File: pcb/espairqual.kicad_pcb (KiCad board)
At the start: 2 copper layers, 81 x 50 mm, 33 parts, among them J1 24VAC, J2 PMSX003, J7 eflashy32, U1 BD9G101G, U2 ESP32-S2-WROVER, U3 AP1117-33

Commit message: hmm
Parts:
- added J3: USB_C_Receptacle_USB2.0, Connector_USB:USB_C_Receptacle_HRO_TYPE-C-31-M-12, F.Cu at (85.6, 76.2)
- added R4: 5k1, Resistor_SMD:R_0805_2012Metric, F.Cu at (77.8, 74.0)
- added R7: 5k1, Resistor_SMD:R_0805_2012Metric, F.Cu at (93.2, 74.0)
- moved L1 0.98 mm to (51.2, 67.6)
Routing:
- net +5V: track 136.8 -> 147.6 mm, vias 3 -> 5
- net GND: track 106.4 -> 117.2 mm, vias 26 -> 30
- net Net-(J3-PadA5): track 0.00 -> 10.7 mm
- net Net-(J3-PadB5): track 0.00 -> 9.93 mm

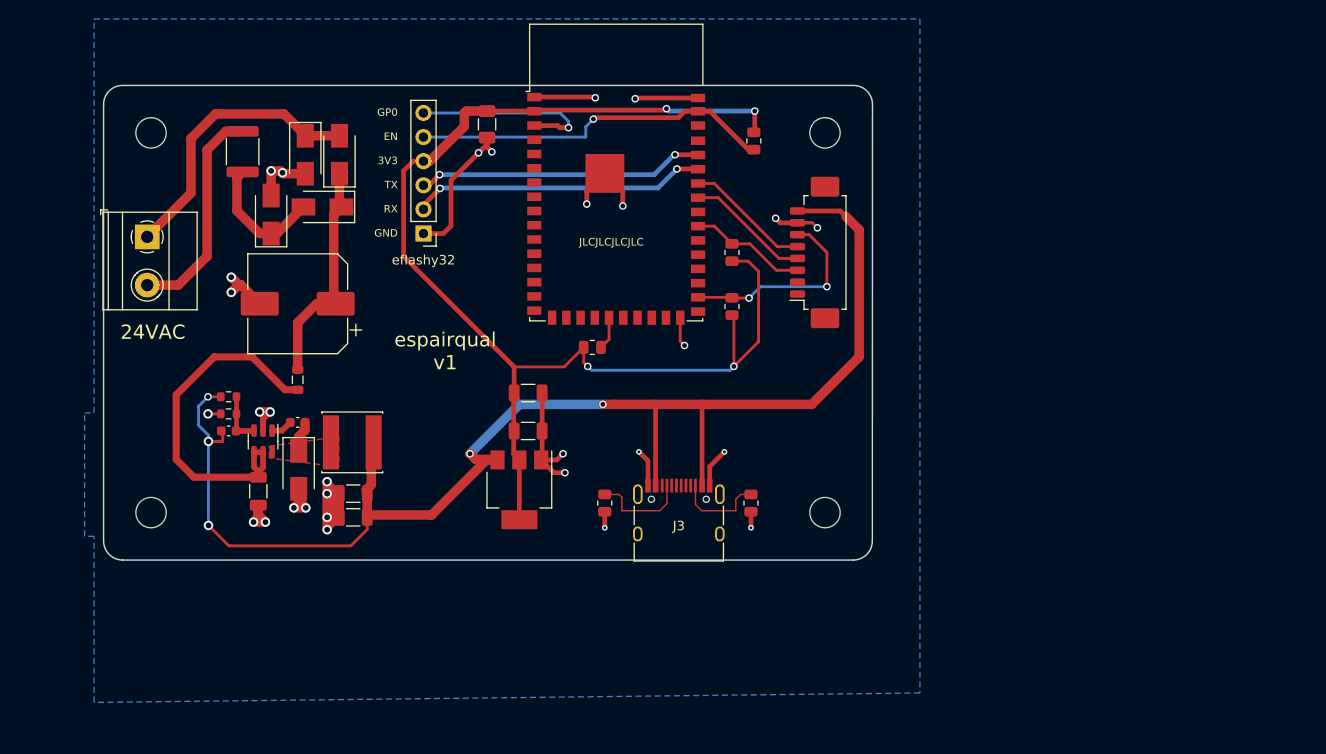
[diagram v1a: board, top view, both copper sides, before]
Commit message: esp32 time
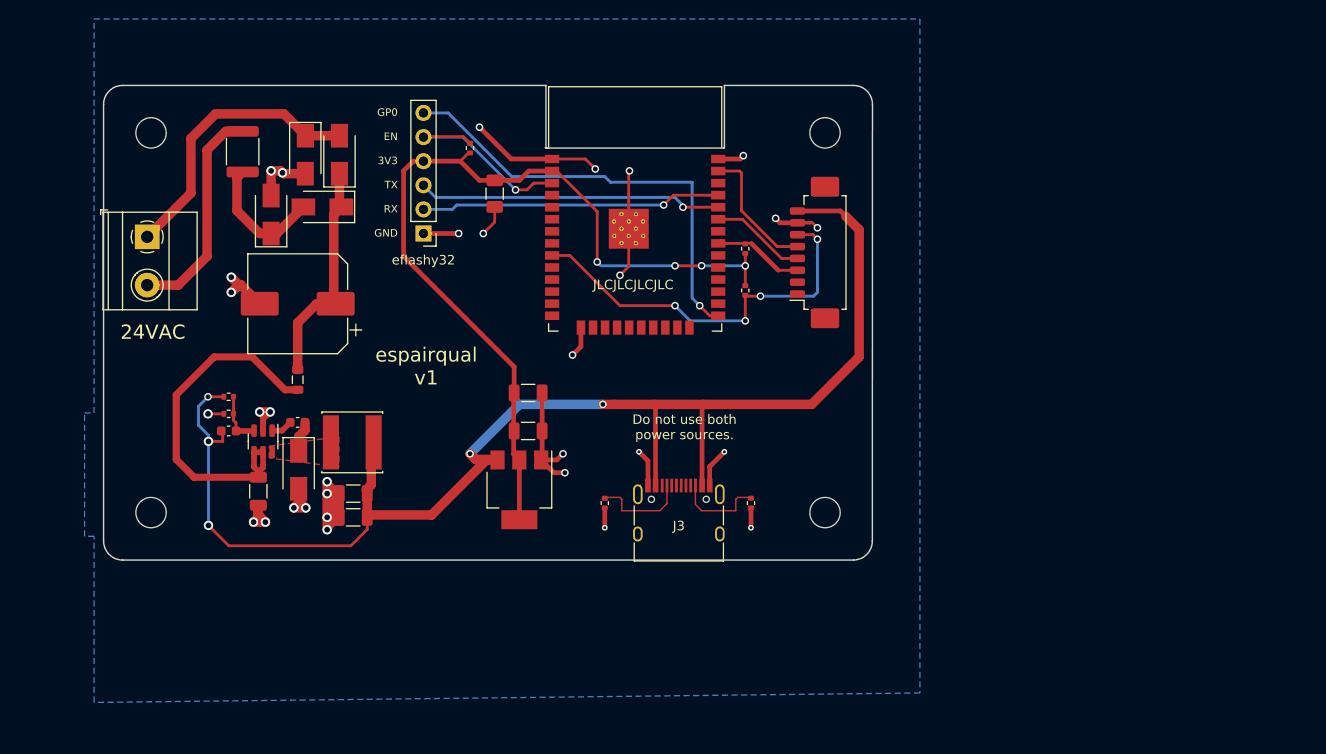
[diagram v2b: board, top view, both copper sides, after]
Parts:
- removed R6: 10K, Resistor_SMD:R_0805_2012Metric
- R1, R3, R4, R5, R7: footprint Resistor_SMD:R_0805_2012Metric -> Resistor_SMD:R_0402_1005Metric
- R12, R2: footprint Resistor_SMD:R_0603_1608Metric -> Resistor_SMD:R_0402_1005Metric
- U2: value ESP32-S2-WROVER -> ESP32-WROOM-32D; footprint RF_Module:ESP32-S2-WROVER -> RF_Module:ESP32-WROOM-32
- U3: value AP1117-33 -> AMS1117-3.3
- moved R5 29.9 mm to (63.6, 36.6), turned to -90 degrees
- moved C7 7.34 mm to (66.2, 41.4)
- moved U2 3.61 mm to (81.0, 46.0)
- moved R3 2.19 mm to (92.6, 51.6), turned to 90 degrees
- moved R1 1.46 mm to (92.6, 47.2)
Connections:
- U2 pad 15: unconnected-(U2-Pad15) -> GND
- U2 pad 21: Net-(R6-Pad1) -> unconnected-(U2-Pad21)
- U2 pad 25: unconnected-(U2-Pad25) -> /GPIO0
- U2 pad 26: GND -> unconnected-(U2-Pad26)
- U2 pad 28: /PMS_SET -> unconnected-(U2-Pad28)
- U2 pad 3: /GPIO0 -> /EN
- U2 pad 31: unconnected-(U2-Pad31) -> /PMS_RESET
- U2 pad 33: /PMS_RESET -> /PMS_TXD
- U2 pad 34: unconnected-(U2-Pad34) -> /TX
- U2 pad 35: /PMS_TXD -> /RX
- U2 pad 36: /PMS_RXD -> unconnected-(U2-Pad36)
- U2 pad 37: /RX -> /PMS_RXD
- U2 pad 38: /TX -> GND
- U2 pad 39: unconnected-(U2-Pad39) -> GND
- U2 pad 9: unconnected-(U2-Pad9) -> /PMS_SET
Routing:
- net +3V3: track 130.7 -> 91.5 mm
- net /GPIO0: track 20.0 -> 47.0 mm
- net /PMS_SET: track 21.6 -> 41.6 mm, vias 2 -> 4
- net /EN: track 38.2 -> 21.3 mm
- net Net-(R6-Pad1): track 3.48 -> 0.00 mm
- net /PMS_TXD: track 13.1 -> 10.1 mm
- net /PMS_RESET: track 12.4 -> 9.52 mm
- net /TX: track 30.3 -> 32.1 mm, vias 2 -> 1
- net GND: track 117.2 -> 116.2 mm, vias 30 -> 31
- net /PMS_RXD: track 13.2 -> 14.0 mm
- net /RX: track 31.0 -> 31.7 mm, vias 2 -> 1
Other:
- outline, holes or cut-outs redrawn
- board text added: "Do not use both power sources."

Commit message: caps
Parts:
- added C10: 10uF 50V, Capacitor_SMD:C_1206_3216Metric, F.Cu at (43.0, 50.1)
- added C11: 10uF 50V, Capacitor_SMD:C_1206_3216Metric, F.Cu at (40.4, 50.1)
- added C12: 10uF 50V, Capacitor_SMD:C_1206_3216Metric, F.Cu at (48.2, 50.1)
- C6: value 470uF 50V -> 10uF 50V; footprint Capacitor_SMD:CP_Elec_10x10 -> Capacitor_SMD:C_1206_3216Metric
- moved FB1 11.1 mm to (37.6, 53.2)
- moved R7 6.21 mm to (89.8, 68.8)
- moved C8 6.21 mm to (66.3, 61.2)
- moved J3 6.21 mm to (82.2, 71.0)
- moved R4 6.21 mm to (74.4, 68.8)
- moved C9 6.21 mm to (66.3, 57.2)
- moved U3 6.21 mm to (65.4, 67.4)
- moved REF** 5.20 mm to (101.0, 69.8)
- moved REF** 5.20 mm to (30.0, 69.8)
- moved C4 5.18 mm to (38.2, 61.2)
- moved C1 5.17 mm to (41.3, 67.6)
- moved C2 5.17 mm to (51.3, 70.3)
- moved C3 5.17 mm to (51.3, 67.8)
- moved C5 5.17 mm to (45.5, 60.3)
- moved D1 5.17 mm to (45.5, 65.3)
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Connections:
- net Net-(C6-Pad1) renamed /Vrec
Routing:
- net Net-(C1-Pad1): track 37.6 -> 28.1 mm
- net +3V3: track 91.5 -> 84.9 mm
- net +5V: track 147.6 -> 141.4 mm
- net GND: track 116.2 -> 121.0 mm
- net /Vrec: track 24.0 -> 25.0 mm
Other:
- board size 81 x 50 mm -> 81 x 44.8 mm

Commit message: update workflow
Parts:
- removed C11, C12: 10uF 50V, Capacitor_SMD:C_1206_3216Metric
- removed REF** (x4): MountingHole_3.2mm_M3, MountingHole:MountingHole_3.2mm_M3
- added C16: 1uF, Capacitor_SMD:C_0603_1608Metric, F.Cu at (71.5, 44.8)
- added H1: MountingHole, MountingHole:MountingHole_3.2mm_M3, F.Cu at (30.0, 75.2)
- added H2: MountingHole, MountingHole:MountingHole_3.2mm_M3, F.Cu at (101.2, 75.2)
- added H3: MountingHole, MountingHole:MountingHole_3.2mm_M3, F.Cu at (30.0, 34.6)
- added H4: MountingHole, MountingHole:MountingHole_3.2mm_M3, F.Cu at (101.2, 34.6)
- C10: value 10uF 50V -> 100uF 50V; footprint Capacitor_SMD:C_1206_3216Metric -> Capacitor_THT:CP_Radial_D10.0mm_P5.00mm_P7.50mm
- moved J2 29.1 mm to (89.0, 74.3), turned to 0 degrees
- moved R7 20.3 mm to (69.5, 68.9), turned to 90 degrees
- moved J1 20.1 mm to (46.1, 34.5), turned to 180 degrees
- moved J3 15.4 mm to (67.9, 76.7)
- moved C10 9.48 mm to (50.0, 56.5)
- moved C6 8.62 mm to (40.3, 56.9)
- moved R4 7.80 mm to (66.6, 68.9), turned to 90 degrees
- moved C8 7.74 mm to (69.8, 54.3)
- moved C9 7.74 mm to (69.8, 50.3)
- moved U3 7.74 mm to (68.9, 60.5)
- moved D3 6.79 mm to (47.5, 49.6)
- moved D4 6.79 mm to (45.8, 44.1)
- moved D5 6.79 mm to (49.4, 44.1)
- moved L1 6.79 mm to (50.7, 69.2)
- moved R12 6.79 mm to (37.7, 64.4)
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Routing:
- net /PMS_RXD: track 14.0 -> 47.8 mm, vias 0 -> 2
- net GND: track 121.0 -> 87.3 mm, vias 31 -> 30
- net /PMS_TXD: track 10.1 -> 42.2 mm, vias 0 -> 2
- net /PMS_RESET: track 9.52 -> 39.4 mm, vias 0 -> 2
- net Net-(D4-Pad1): track 30.0 -> 11.3 mm
- net Net-(F1-Pad1): track 23.3 -> 7.91 mm
- net +3V3: track 84.9 -> 74.6 mm
- net +5V: track 141.4 -> 131.7 mm, vias 5 -> 7
- net Net-(J3-PadA5): track 10.5 -> 2.57 mm
- net Net-(J3-PadB5): track 9.83 -> 2.61 mm
- net /Vrec: track 25.0 -> 29.1 mm
- net /PMS_SET: track 41.6 -> 45.6 mm, vias 4 -> 2
- net /GPIO0: track 47.0 -> 43.4 mm
- net /RX: track 31.7 -> 28.9 mm
- net /TX: track 32.1 -> 29.5 mm
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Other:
- board size 81 x 44.8 mm -> 98 x 50 mm
- board text added: "24VAC 100uF 18VAC 220uF"
- board text added: "Hammond 1593"
- board text added: "espairqual v2"
- board text removed: "espairqual v1"

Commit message: changes
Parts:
- removed C16: 1uF, Capacitor_SMD:C_0603_1608Metric
- removed C2, C3: 47u, Capacitor_SMD:C_1206_3216Metric
- removed R7: 5k1, Resistor_SMD:R_0402_1005Metric
- removed U2: ESP32-WROOM-32D, RF_Module:ESP32-WROOM-32
- added C11: 10uF 50V, Capacitor_SMD:C_1206_3216Metric, F.Cu at (76.6, 39.4)
- added C12: 10uF 50V, Capacitor_SMD:C_1206_3216Metric, F.Cu at (68.1, 36.9)
- added D6: SS210, Diode_SMD:D_SMA, F.Cu at (41.2, 45.6)
- added D7: SS210, Diode_SMD:D_SMA, F.Cu at (37.2, 81.8)
- added D8: PWR, LED_SMD:LED_0805_2012Metric, F.Cu at (44.2, 63.8)
- added J4: USBC, Connector_USB:USB_C_Receptacle_GCT_USB4105-xx-A_16P_TopMnt_Horizontal, F.Cu at (54.1, 33.5)
- added J5: GCJA5, Connector_JST:JST_GH_SM05B-GHS-TB_1x05-1MP_P1.25mm_Horizontal, F.Cu at (47.2, 91.4)
- added J6: TEST, Connector_PinHeader_2.54mm:PinHeader_1x04_P2.54mm_Vertical, F.Cu at (28.5, 96.2)
- added R10: 5k1, Resistor_SMD:R_0402_1005Metric, F.Cu at (57.0, 44.0)
- added R11: 5k1, Resistor_SMD:R_0402_1005Metric, F.Cu at (51.2, 44.0)
- added R6: 680, Resistor_SMD:R_0402_1005Metric, F.Cu at (40.8, 63.8)
- added SW1: RESET, Button_Switch_SMD:SW_Push_1P1T_XKB_TS-1187A, F.Cu at (62.8, 35.8)
- added TP1: +5V, TestPoint:TestPoint_Pad_D2.5mm, B.Cu at (43.8, 83.2)
- added TP2: GND, TestPoint:TestPoint_Pad_D2.5mm, B.Cu at (69.2, 83.2)
- added TP3: +3.3V, TestPoint:TestPoint_Pad_D2.5mm, B.Cu at (74.8, 83.2)
- added U4: ESP32-C3-MINI-1, Espressif:ESP32-C3-MINI-1, F.Cu at (75.4, 49.7)
- C1, C7, C8, C9: value 10u -> 10uF 50V
- C10: footprint Capacitor_THT:CP_Radial_D10.0mm_P5.00mm_P7.50mm -> Capacitor_SMD:CP_Elec_8x10
- J3: value USB_C_Receptacle_USB2.0 -> eflashy32; footprint Connector_USB:USB_C_Receptacle_HRO_TYPE-C-31-M-12 -> Connector_PinHeader_2.54mm:PinHeader_1x06_P2.54mm_Vertical
- J7: value eflashy32 -> AUX; footprint Connector_PinHeader_2.54mm:PinHeader_1x06_P2.54mm_Vertical -> Connector_PinHeader_2.54mm:PinHeader_1x05_P2.54mm_Vertical_SMD_Pin1Left; moved to B.Cu
- L1: footprint Inductor_SMD:L_Sunlord_SWPA60xxS -> Inductor_SMD:L_Sunlord_SWPA5012S
- R1, R3, R5: value 10K -> 5k1
- moved C7 56.5 mm to (32.4, 82.8)
- moved J7 38.5 mm to (55.7, 83.1), turned to -90 degrees
- moved J2 29.6 mm to (64.8, 91.2)
- moved H2 28.1 mm to (80.3, 94.2)
- moved R4 27.9 mm to (73.0, 41.7), turned to 0 degrees
- moved R3 27.2 mm to (73.6, 35.4), turned to 180 degrees
- moved R1 27.1 mm to (71.1, 35.4), turned to 180 degrees
- moved L1 26.5 mm to (27.8, 82.6), turned to -90 degrees
- moved H1 21.3 mm to (20.4, 94.2)
- moved R5 21.0 mm to (59.0, 55.5), turned to 0 degrees
- moved C10 20.9 mm to (29.1, 57.9)
- moved H4 20.8 mm to (80.3, 34.1)
- moved D2 20.4 mm to (21.8, 51.2), turned to -90 degrees
- moved C9 20.2 mm to (52.2, 60.1), turned to 180 degrees
- moved C8 20.0 mm to (52.2, 63.6), turned to 180 degrees
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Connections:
- C4 pad 1: +5V -> Net-(D7-A)
- C7 pad 1: GND -> Net-(D7-A)
- C7 pad 2: +3V3 -> GND
- J2 pad 3: /PMS_RESET -> /GPIO3
- J2 pad 6: /PMS_SET -> /GPIO5
- J7 pad 1: GND -> /GPIO10
- J7 pad 2: /RX -> /GPIO7
- J7 pad 3: /TX -> /GPIO6
- J7 pad 4: +3V3 -> /GPIO5
- J7 pad 5: /EN -> /GPIO3
- L1 pad 2: +5V -> Net-(D7-A)
- R1 pad 1: /PMS_RESET -> Net-(R1-Pad1)
- R1 pad 2: +3V3 -> /EN
- R12 pad 2: +5V -> Net-(D7-A)
- R3 pad 1: /PMS_SET -> +3V3
- R3 pad 2: +3V3 -> Net-(R1-Pad1)
- R4 pad 1: Net-(J3-PadA5) -> +3V3
- R4 pad 2: GND -> Net-(U4-GPIO2/ADC1_CH2)
- R5 pad 1: /EN -> +3V3
- R5 pad 2: +3V3 -> Net-(U4-GPIO8)
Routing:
- net /GPIO6: track 0.00 -> 76.3 mm, vias 0 -> 5
- net /GPIO7: track 0.00 -> 75.5 mm, vias 0 -> 7
- net /GPIO10: track 0.00 -> 73.2 mm, vias 0 -> 3
- net /GPIO3: track 0.00 -> 55.2 mm, vias 0 -> 3
- net /GPIO5: track 0.00 -> 50.4 mm, vias 0 -> 4
- net D+: track 0.00 -> 46.9 mm
- net /PMS_SET: track 45.6 -> 0.00 mm, vias 2 -> 0
- net D-: track 0.00 -> 43.8 mm, vias 0 -> 2
- net /PMS_RESET: track 39.4 -> 0.00 mm, vias 2 -> 0
- net +5V: track 131.7 -> 93.7 mm, vias 7 -> 4
- net Net-(D7-A): track 0.00 -> 34.6 mm, vias 0 -> 2
- net +3V3: track 74.6 -> 105.9 mm, vias 4 -> 9
- net /TX: track 29.5 -> 0.00 mm, vias 1 -> 0
- net /RX: track 28.9 -> 0.00 mm, vias 1 -> 0
- net /EN: track 21.5 -> 49.3 mm, vias 1 -> 4
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- added copper zone on F.Cu, net GND
- added copper zone on F.Cu, net Net-(U1-EN)
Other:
- board size 98 x 50 mm -> 67.5 x 68.5 mm
- board text added: "GCJA5"
- board text added: "GPIO10 GPIO GPIO3"
- board text added: "GPIO7 GPIO5"
- board text added: "Hammond 1593ARBK"
- board text added: "PMSx003"
- board text added: "UART SDA SCL GND"
- board text added: "espairqual v3"
- board text removed: "24VAC 100uF 18VAC 220uF"
- board text removed: "Do not use both power sources."
- board text removed: "GP0 EN 3V3 TX RX GND"
- board text removed: "Hammond 1593"
- board text removed: "espairqual v2"

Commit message: tweak
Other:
- board text added: "espairqual v3.0 github.com/gcormier/espairqual"
- board text removed: "espairqual v3"
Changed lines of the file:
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@@
     (effects (font (size 1 1) (thickness 0.15)) (justify left bottom mirror))
   )
-  (gr_text "espairqual\nv3" (at 53.5 70.25) (layer "F.SilkS")
+  (gr_text "espairqual\nv3.0\ngithub.com/gcormier/espairqual" (at 53.5 70.25) (layer "F.SilkS")
     (effects (font (size 1.5 1.5) (thickness 0.3)))
   )

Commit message: touchup before fab
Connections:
- J5 pad 2: GND -> /GPIO6
- J5 pad 4: /GPIO6 -> GND
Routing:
- net /GPIO0: track 49.3 -> 55.3 mm
- net /GPIO6: track 76.3 -> 77.3 mm, vias 5 -> 7

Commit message: updates
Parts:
- removed J6: TEST, Connector_PinHeader_2.54mm:PinHeader_1x04_P2.54mm_Vertical
- moved H3 90.7 mm to (109.4, 51.1)
- moved H1 90.3 mm to (109.4, 79.1)
- moved R10 90.0 mm to (146.9, 46.8)
- moved J4 89.9 mm to (143.8, 39.8)
- moved R11 85.5 mm to (136.6, 40.7), turned to 180 degrees
- moved R6 81.4 mm to (120.6, 79.3), turned to 90 degrees
- moved D6 80.0 mm to (117.6, 69.3)
- moved D8 79.6 mm to (121.6, 82.3)
- moved J5 78.4 mm to (125.6, 90.6)
- moved U3 77.3 mm to (126.0, 69.0)
- moved C8 77.3 mm to (128.1, 78.3)
- moved C9 77.3 mm to (128.1, 74.8)
- moved J2 76.4 mm to (141.2, 90.8)
- moved J3 76.3 mm to (149.6, 54.1), turned to 0 degrees
- moved F1 76.1 mm to (97.7, 43.3)
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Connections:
- net Net-(D6-A) renamed /PWR5V
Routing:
- net /PWR5V: track 23.4 -> 58.7 mm, vias 2 -> 5
- net /GPIO6: track 77.3 -> 45.7 mm, vias 7 -> 3
- net /GPIO7: track 75.5 -> 47.5 mm, vias 7 -> 3
- net D+: track 46.9 -> 26.4 mm
- net D-: track 43.8 -> 23.5 mm
- net /GPIO0: track 55.3 -> 35.7 mm, vias 6 -> 0
- net /GPIO10: track 73.2 -> 55.0 mm
- net /PMS_RXD: track 46.1 -> 61.9 mm, vias 0 -> 3
- net /PMS_TXD: track 47.4 -> 61.1 mm, vias 2 -> 3
- net GND: track 98.6 -> 109.8 mm, vias 40 -> 56
- net /GPIO3: track 55.2 -> 65.6 mm, vias 3 -> 4
- net /GPIO5: track 50.4 -> 60.3 mm, vias 4 -> 2
- net +3V3: track 105.9 -> 98.5 mm, vias 9 -> 3
- net Net-(D7-A): track 34.6 -> 42.0 mm
- net Net-(D2-K): track 8.96 -> 14.8 mm
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- added copper zone on In1.Cu, net GND
- added copper zone on In2.Cu, net GND
- removed copper zone on B.Cu, net GND
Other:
- board size 67.5 x 68.5 mm -> 56.6 x 57.7 mm
- copper layers 2 -> 4
- board text added: "GPIO10 GPIO6 GPIO3"
- board text added: "Hammond 1593KBK"
- board text removed: "GPIO10 GPIO GPIO3"
- board text removed: "Hammond 1593ARBK"
- board text removed: "J3"
- board text removed: "UART SDA SCL GND"
